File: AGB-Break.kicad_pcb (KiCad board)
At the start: 2 copper layers, 71.4 x 86.7 mm, 40 parts, among them J1 CONN_WII, J2 Conn_02x03_Odd_Even, SW1 SW_Push, U1 AGB-CPU, U2 ATmega328P-AU, U3 TS5A3160DBV, U4 AGB_SRAM, U5 SpartanEdge, U6 LP5907MFX-2.5, U7 GBA-Slot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

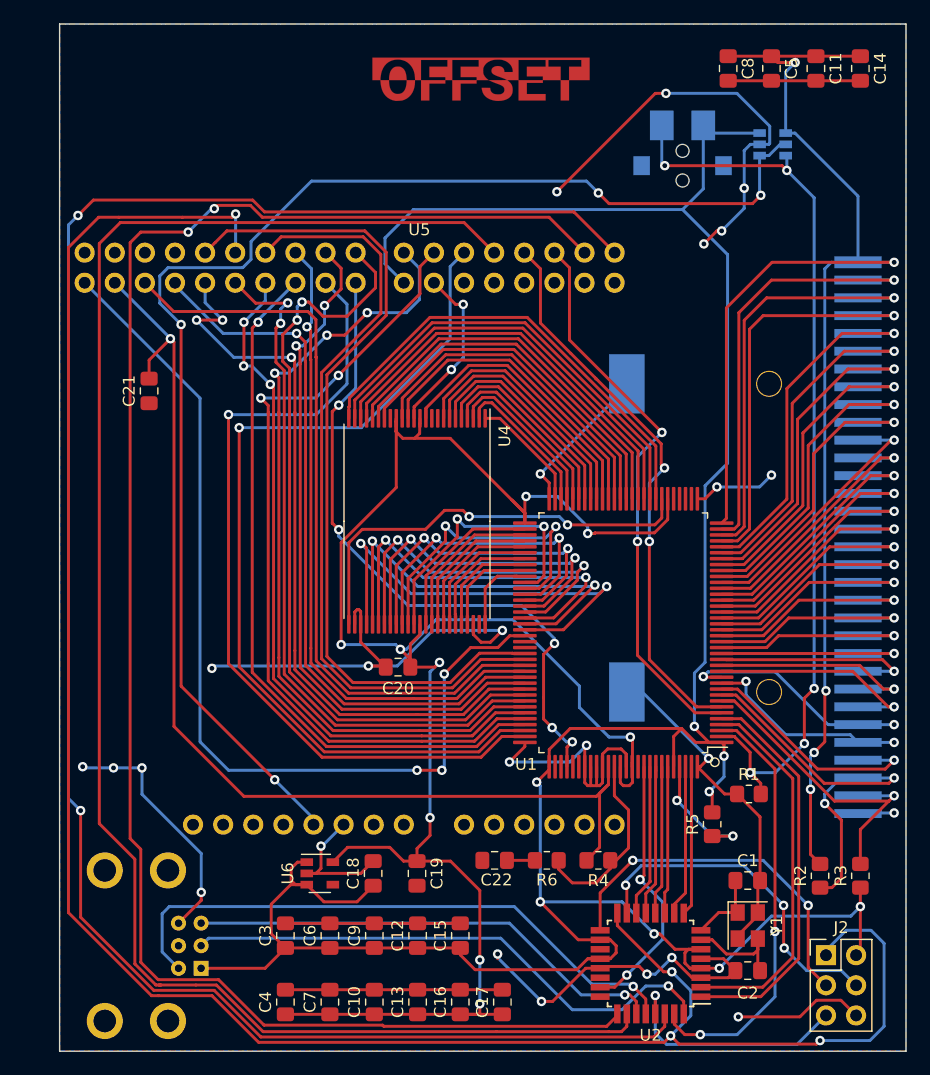
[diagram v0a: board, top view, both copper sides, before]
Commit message: Finished current routing, still missing power switch.
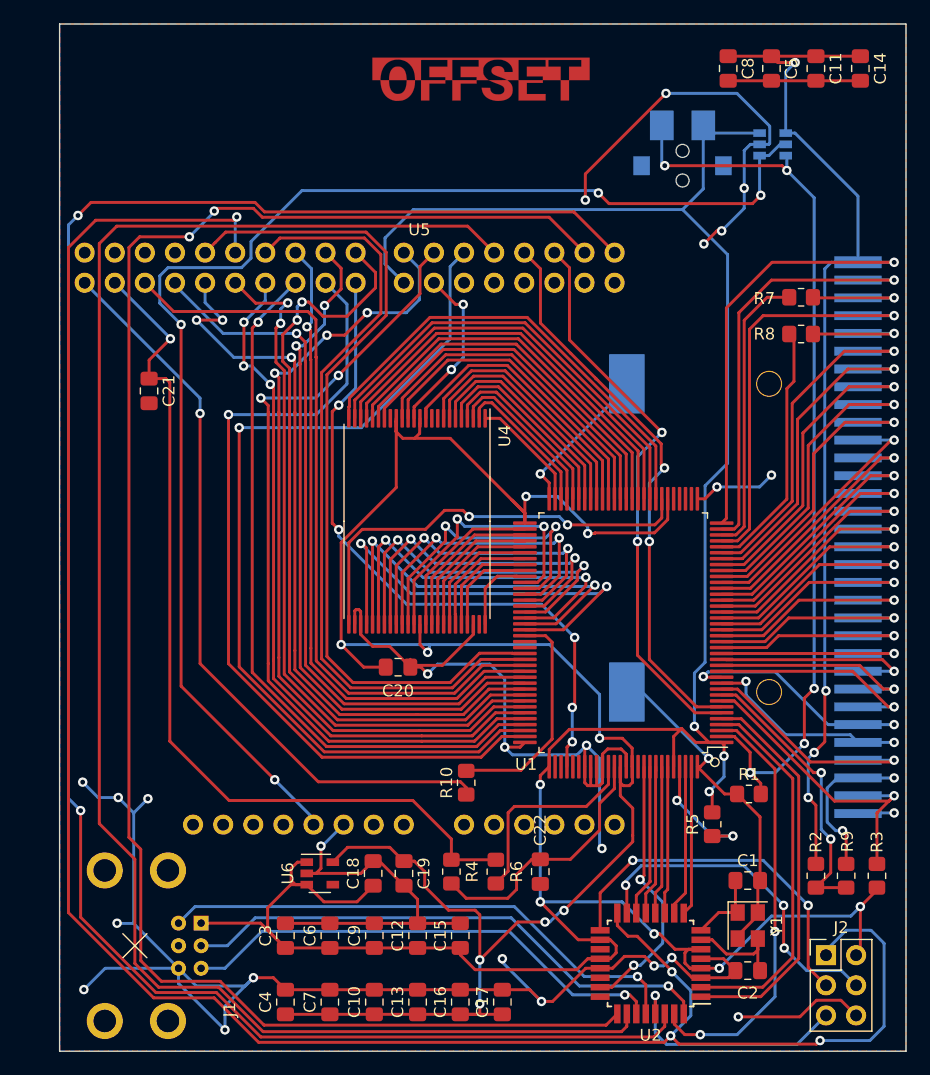
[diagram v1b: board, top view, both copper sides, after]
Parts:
- added R10: 270, Resistor_SMD:R_0805_2012Metric_Pad1.20x1.40mm_HandSolder, F.Cu at (166.8, 93.2)
- added R7: 47, Resistor_SMD:R_0805_2012Metric_Pad1.20x1.40mm_HandSolder, F.Cu at (195.0, 52.3)
- added R8: 47, Resistor_SMD:R_0805_2012Metric_Pad1.20x1.40mm_HandSolder, F.Cu at (195.0, 55.4)
- added R9: 15, Resistor_SMD:R_0805_2012Metric_Pad1.20x1.40mm_HandSolder, F.Cu at (198.8, 101.1)
- J1: moved to F.Cu
- moved R4 12.4 mm to (165.5, 100.8), turned to 270 degrees
- moved R6 4.40 mm to (169.2, 100.8), turned to 90 degrees
- moved C22 3.97 mm to (173.0, 100.8), turned to 90 degrees
- moved R3 1.40 mm to (201.4, 101.1)
- moved C19 1.10 mm to (161.5, 100.9)
- moved R2 0.35 mm to (196.2, 101.1)
- turned C20 to 180 degrees
- turned C21 to 270 degrees
- turned J1 to 90 degrees
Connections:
- C10 pad 2: Net-(C10-Pad2) -> GND
- C11 pad 2: Net-(C11-Pad2) -> GND
- C12 pad 2: Net-(C12-Pad2) -> GND
- C13 pad 2: Net-(C10-Pad2) -> GND
- C14 pad 2: Net-(C11-Pad2) -> GND
- C15 pad 2: Net-(C12-Pad2) -> GND
- C16 pad 2: Net-(C10-Pad2) -> GND
- C17 pad 2: Net-(C10-Pad2) -> GND
- C21 pad 1: GND -> GBA_CLK
- C21 pad 2: GBA_CLK -> GND
- C22 pad 1: Net-(C22-Pad1) -> GND
- C22 pad 2: GND -> Net-(C22-Pad2)
- C3 pad 2: Net-(C12-Pad2) -> GND
- C4 pad 2: Net-(C10-Pad2) -> GND
- C5 pad 2: Net-(C11-Pad2) -> GND
- C6 pad 2: Net-(C12-Pad2) -> GND
- C7 pad 2: Net-(C10-Pad2) -> GND
- C8 pad 2: Net-(C11-Pad2) -> GND
- C9 pad 2: Net-(C12-Pad2) -> GND
- R4 pad 2: Net-(R4-Pad2) -> Net-(C22-Pad2)
- R6 pad 1: Net-(C22-Pad1) -> Net-(R6-Pad1)
- R6 pad 2: Net-(R4-Pad2) -> GBA_CLK
- U1 pad 113: GBA_CLK -> Net-(R6-Pad1)
- U1 pad 114: Net-(R4-Pad2) -> Net-(C22-Pad2)
- U1 pad 84: LCD_DCLK -> Net-(R10-Pad2)
- U7 pad 3: CART_WR -> Net-(R7-Pad2)
- U7 pad 30: CART_RES -> Net-(R9-Pad2)
- U7 pad 5: CART_CS -> Net-(R8-Pad2)
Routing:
- net GND: track 237.5 -> 326.9 mm, vias 27 -> 29
- net Net-(C22-Pad2): track 0.00 -> 22.0 mm
- net Net-(R10-Pad2): track 0.00 -> 19.1 mm
- net Net-(C10-Pad2): track 18.3 -> 0.00 mm
- net Net-(R6-Pad1): track 0.00 -> 17.3 mm
- net LCD_DCLK: track 80.5 -> 63.5 mm, vias 3 -> 1
- net GBA_CLK: track 91.8 -> 75.6 mm
- net Net-(R4-Pad2): track 16.1 -> 0.00 mm
- net Net-(C12-Pad2): track 14.8 -> 0.00 mm
- net Net-(R9-Pad2): track 0.00 -> 13.9 mm, vias 0 -> 2
- net CART_WR: track 36.6 -> 24.2 mm, vias 1 -> 0
- net Net-(C11-Pad2): track 11.2 -> 0.00 mm
- net Net-(R8-Pad2): track 0.00 -> 10.4 mm, vias 0 -> 1
- net Net-(R7-Pad2): track 0.00 -> 10.4 mm, vias 0 -> 1
- net CART_RES: track 34.6 -> 24.2 mm
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
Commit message: Finished PCB v1
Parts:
- added D1: LED, LED_THT:LED_D5.0mm_FlatTop, F.Cu at (144.0, 36.5)
- added J3: Conn_01x02, Connector_PinSocket_2.54mm:PinSocket_1x02_P2.54mm_Vertical, F.Cu at (134.8, 43.8)
- added R11: 120, Resistor_SMD:R_0805_2012Metric_Pad1.20x1.40mm_HandSolder, F.Cu at (151.0, 35.2)
- added REF**: MountingHole_2.2mm_M2, MountingHole:MountingHole_2.2mm_M2, F.Cu at (144.0, 41.2)
- added REF**: MountingHole_2.2mm_M2, MountingHole:MountingHole_2.2mm_M2, F.Cu at (149.0, 100.8)
- added REF**: MountingHole_2.2mm_M2, MountingHole:MountingHole_2.2mm_M2, F.Cu at (191.8, 113.2)
- added REF**: MountingHole_2.2mm_M2, MountingHole:MountingHole_2.2mm_M2, F.Cu at (199.8, 38.5)
- added U8: Switch-DPDT, Raizu_OFFSET:XKB_XKB5858-Z-C, F.Cu at (137.2, 35.2)
- G***: footprint Raizu_OFFSET:OFFSET_LOGO_4.0mm -> Raizu_OFFSET:OFFSET_LOGO_6.2mm
- U2: value ATmega328P-AU -> ATmega328PB-AU
- U4: footprint Gekkio_Package_SO:TSOP-I-48_16.4x12mm_P0.5mm -> Raizu_OFFSET:AGB_SRAM
- moved G*** 3.66 mm to (168.2, 37.8)
- moved SW1 0.30 mm to (185.0, 40.5)
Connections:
- U2 pad 3: GND -> Net-(U2-Pad3)
- U2 pad 6: +3V3 -> Net-(U2-Pad6)
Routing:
- net /PWR_5V: track 0.00 -> 21.4 mm
- net GND: track 326.9 -> 306.3 mm
- net Net-(D1-Pad1): track 0.00 -> 7.93 mm
- net /PWR_VIN: track 0.00 -> 7.91 mm
- net +3V3: track 238.7 -> 234.0 mm
- net RAM_WE: track 23.8 -> 26.7 mm
- net RAM_LB: track 28.2 -> 31.0 mm
- net RAM_UB: track 26.7 -> 29.5 mm
- net /A01: track 39.3 -> 42.1 mm
- net /A02: track 37.8 -> 40.6 mm
- net /A03: track 36.3 -> 39.1 mm
- net /A04: track 34.8 -> 37.5 mm
- net /A05: track 33.2 -> 36.0 mm
- net /A06: track 31.7 -> 34.5 mm
- net /A07: track 30.2 -> 32.9 mm
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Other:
- board text added: "5V"
- board text added: "VIN"

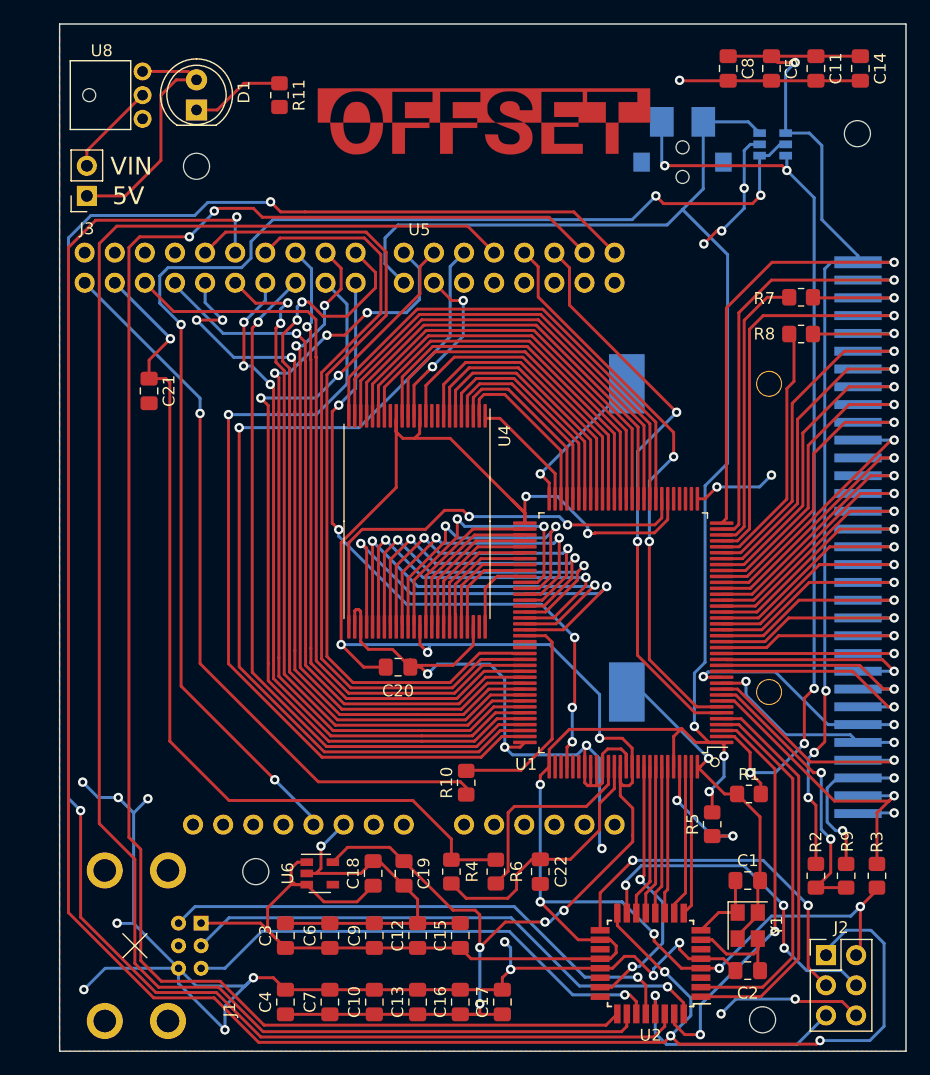
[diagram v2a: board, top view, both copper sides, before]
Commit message: Finished PCB work, but headers are flipped, need to fix this :(
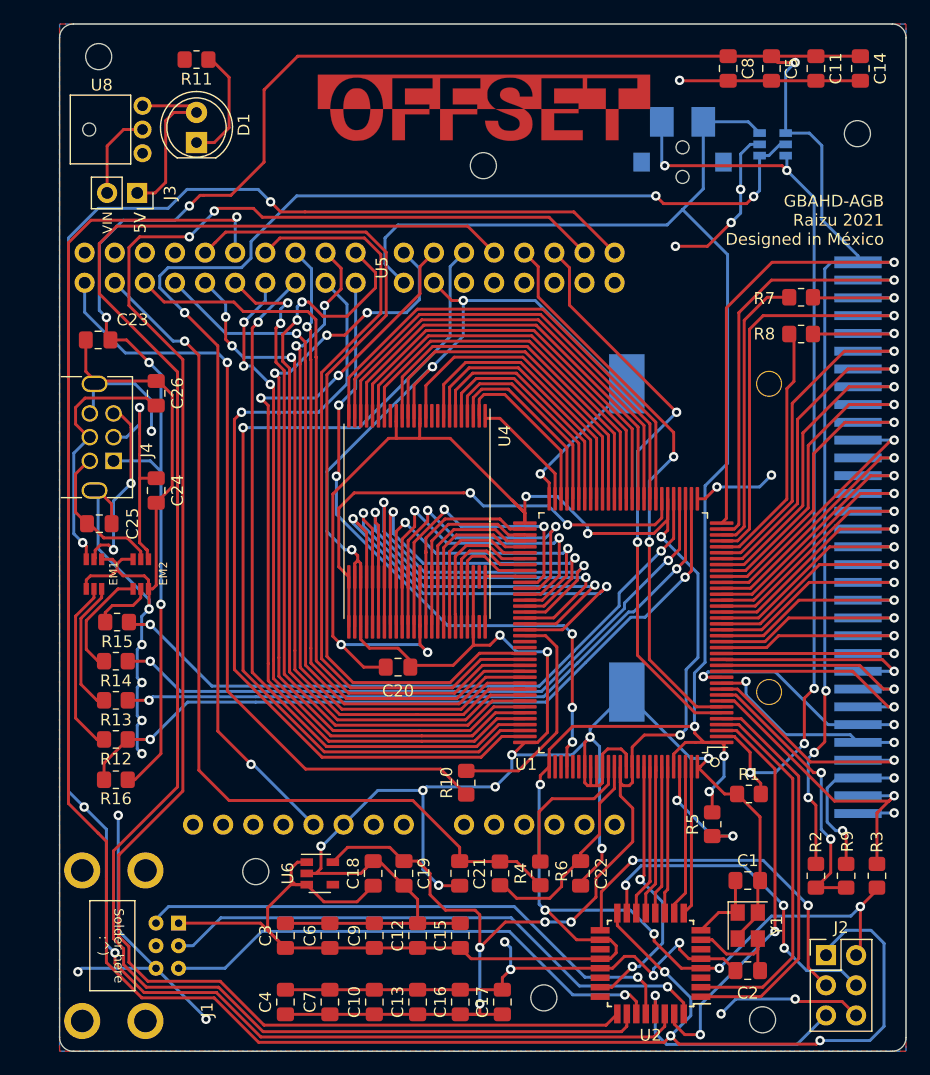
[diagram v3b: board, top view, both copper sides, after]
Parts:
- removed the REF** at (144.0, 41.2)
- added C23: 100nF, Capacitor_SMD:C_0805_2012Metric_Pad1.18x1.45mm_HandSolder, F.Cu at (135.7, 55.9)
- added C24: 0.1nF, Capacitor_SMD:C_0805_2012Metric_Pad1.18x1.45mm_HandSolder, F.Cu at (140.6, 68.6)
- added C25: 0.1nF, Capacitor_SMD:C_0805_2012Metric_Pad1.18x1.45mm_HandSolder, F.Cu at (135.8, 71.4)
- added C26: 0.1nF, Capacitor_SMD:C_0805_2012Metric_Pad1.18x1.45mm_HandSolder, F.Cu at (140.6, 60.4)
- added EM1: EMI_Filter_3, Raizu_OFFSET:Inductor-1008-3P, F.Cu at (135.3, 75.6)
- added EM2: EMI_Filter_3, Raizu_OFFSET:Inductor-1008-3P, F.Cu at (139.3, 75.6)
- added G***: LOGO, Raizu_OFFSET:gbahd_logo, B.Cu at (161.0, 72.6)
- added J4: GameBoy_LinkPort, Gekkio_Connector:GameBoy_LinkPort_MGB_Horizontal, F.Cu at (137.0, 66.1)
- added R12: 330, Resistor_SMD:R_0805_2012Metric_Pad1.20x1.40mm_HandSolder, F.Cu at (137.2, 89.6)
- added R13: 330, Resistor_SMD:R_0805_2012Metric_Pad1.20x1.40mm_HandSolder, F.Cu at (137.2, 86.3)
- added R14: 330, Resistor_SMD:R_0805_2012Metric_Pad1.20x1.40mm_HandSolder, F.Cu at (137.2, 83.0)
- added R15: 330, Resistor_SMD:R_0805_2012Metric_Pad1.20x1.40mm_HandSolder, F.Cu at (137.3, 79.7)
- added R16: 100k, Resistor_SMD:R_0805_2012Metric_Pad1.20x1.40mm_HandSolder, F.Cu at (137.2, 93.0)
- added REF**: MountingHole_2.2mm_M2, MountingHole:MountingHole_2.2mm_M2, F.Cu at (173.3, 111.4)
- added REF**: MountingHole_2.2mm_M2, MountingHole:MountingHole_2.2mm_M2, F.Cu at (168.2, 41.2)
- added REF**: MountingHole_2.2mm_M2, MountingHole:MountingHole_2.2mm_M2, F.Cu at (135.8, 32.0)
- moved C21 48.4 mm to (166.2, 100.9)
- moved R11 7.62 mm to (144.0, 32.2), turned to 180 degrees
- moved J3 4.26 mm to (139.0, 43.5), turned to 270 degrees
- moved R4 4.10 mm to (169.6, 100.9)
- moved R6 3.75 mm to (173.0, 100.9), turned to 270 degrees
- moved C22 3.40 mm to (176.4, 100.9)
- moved U8 2.90 mm to (137.2, 38.1)
- moved D1 2.75 mm to (144.0, 39.2)
- moved J1 1.90 mm to (136.9, 107.0)
- moved G*** 1.15 mm to (168.2, 36.6)
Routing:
- net GND: track 306.3 -> 450.3 mm, vias 29 -> 36
- net CART_VCC: track 126.0 -> 243.5 mm, vias 5 -> 9
- net Net-(R12-Pad1): track 0.00 -> 63.7 mm, vias 0 -> 2
- net Net-(R15-Pad1): track 0.00 -> 57.3 mm, vias 0 -> 2
- net Net-(R13-Pad1): track 0.00 -> 57.1 mm, vias 0 -> 2
- net Net-(R14-Pad1): track 0.00 -> 57.1 mm, vias 0 -> 2
- net Net-(C26-Pad1): track 0.00 -> 22.3 mm, vias 0 -> 1
- net Net-(C24-Pad1): track 0.00 -> 18.6 mm, vias 0 -> 1
- net Net-(EM1-Pad2): track 0.00 -> 15.7 mm, vias 0 -> 2
- net Net-(EM1-Pad5): track 0.00 -> 14.7 mm
- net Net-(C25-Pad1): track 0.00 -> 13.0 mm
- net Net-(EM1-Pad4): track 0.00 -> 11.3 mm
- net Net-(EM2-Pad6): track 0.00 -> 9.40 mm
- net +2V5: track 169.4 -> 178.6 mm, vias 9 -> 10
- net /D01: track 31.7 -> 38.3 mm
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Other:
- outline, holes or cut-outs redrawn
- board text added: "GBAHD-AGB Raizu 2021 Designed in México"
- board text added: "JLCJLCJLCJLC"
- board text added: "Solder here :^)"

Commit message: Finished PCB layout, sent to pcb fab.
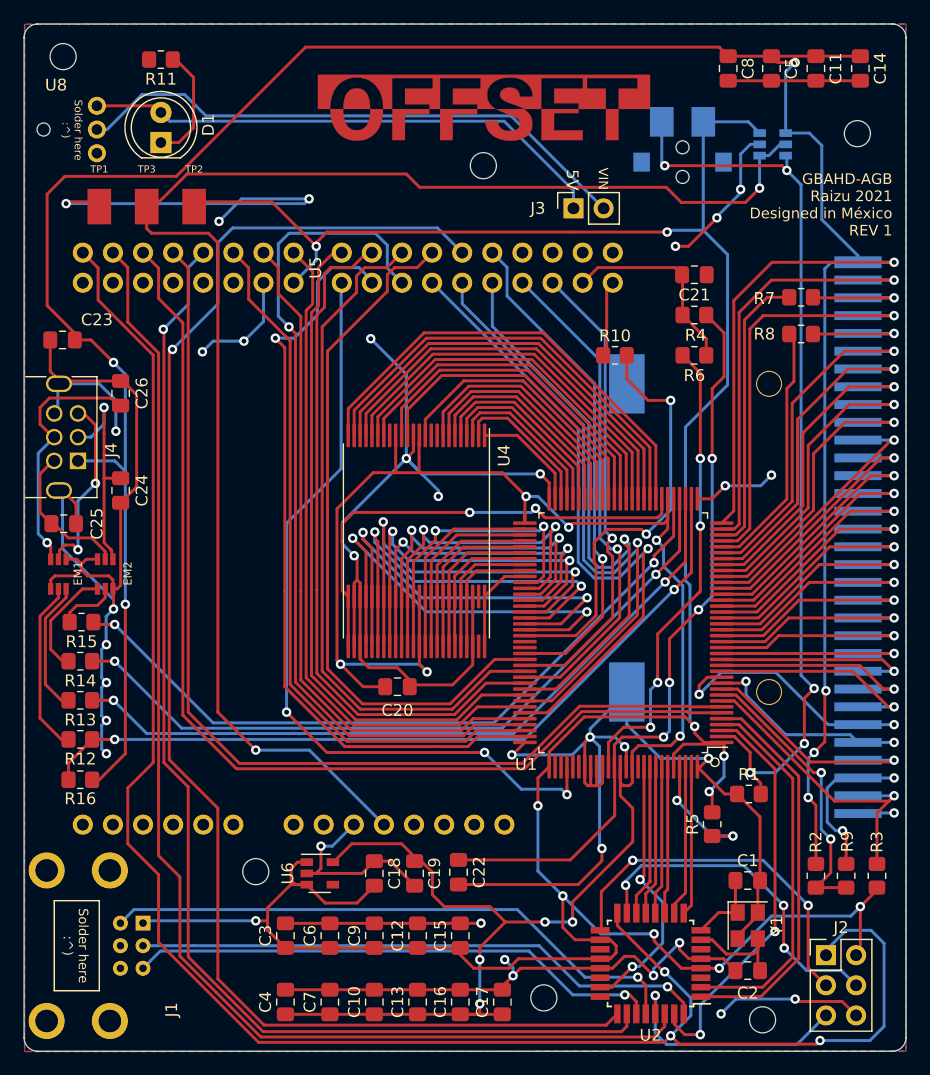
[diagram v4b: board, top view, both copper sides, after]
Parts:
- added TP1: GND, Raizu_OFFSET:SOLDER_PAD, F.Cu at (135.8, 44.5)
- added TP2: 3.3V, Raizu_OFFSET:SOLDER_PAD, F.Cu at (143.8, 44.5)
- added TP3: 5V, Raizu_OFFSET:SOLDER_PAD, F.Cu at (139.8, 44.5)
- U5: moved to B.Cu
- moved C21 54.2 mm to (186.0, 50.4), turned to 0 degrees
- moved R4 49.9 mm to (186.0, 53.8), turned to 0 degrees
- moved R6 45.6 mm to (186.0, 57.2), turned to 0 degrees
- moved R10 38.2 mm to (179.3, 57.2), turned to 0 degrees
- moved J3 36.8 mm to (175.8, 44.8), turned to 90 degrees
- moved C22 10.3 mm to (166.1, 100.8)
- moved U8 3.85 mm to (133.4, 38.1)
- moved C23 3.00 mm to (132.7, 55.9)
- moved C24 3.00 mm to (137.6, 68.6)
- moved C25 3.00 mm to (132.8, 71.4)
- moved C26 3.00 mm to (137.6, 60.4)
- moved D1 3.00 mm to (141.0, 39.2)
- moved EM1 3.00 mm to (132.3, 75.6)
- moved EM2 3.00 mm to (136.3, 75.6)
- moved J1 3.00 mm to (133.9, 107.0)
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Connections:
- U2 pad 25: OSD_CLK -> OSD_LATCH
- U2 pad 30: OSD_DATA -> OSD_CLK
- U5 pad 12: ICSP_MISO -> OSD_LATCH
- U5 pad 28: OSD_DATA -> ICSP_MISO
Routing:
- net OSD_DATA: track 163.2 -> 0.00 mm, vias 3 -> 0
- net OSD_LATCH: track 0.00 -> 123.2 mm, vias 0 -> 1
- net GBA_CLK: track 78.1 -> 16.8 mm, vias 1 -> 0
- net LCD_DCLK: track 67.8 -> 6.64 mm, vias 1 -> 0
- net Net-(C22-Pad2): track 18.0 -> 63.8 mm, vias 0 -> 4
- net OSD_ENABLE: track 147.0 -> 102.5 mm, vias 0 -> 1
- net GND: track 450.3 -> 406.1 mm, vias 36 -> 35
- net OSD_CLK: track 149.9 -> 106.8 mm, vias 2 -> 0
- net GBA_AUD1: track 48.7 -> 89.8 mm, vias 2 -> 0
- net /PWR_VIN: track 7.53 -> 47.9 mm
- net GBA_AUD2: track 48.2 -> 88.1 mm, vias 2 -> 0
- net LCD_R5: track 71.5 -> 42.4 mm, vias 0 -> 1
- net /PWR_5V: track 15.6 -> 44.7 mm
- net Net-(R6-Pad1): track 12.2 -> 40.1 mm, vias 0 -> 4
- net LCD_R3: track 64.2 -> 39.7 mm, vias 0 -> 1
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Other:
- board size 71.4 x 86.7 mm -> 74.4 x 86.7 mm
- board text added: "GBAHD-AGB Raizu 2021 Designed in México REV 1"
- board text removed: "GBAHD-AGB Raizu 2021 Designed in México"
